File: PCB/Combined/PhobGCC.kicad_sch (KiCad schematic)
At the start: 74 parts, among them J1 Conn_01x06_Female, J2 Conn_01x04_Female, J3 Conn_01x01_Male, J4 Conn_01x04_Male, Q1 Q_NMOS_GSD, Q2 Q_PMOS_GDS, Q3 Q_NMOS_GSD, SW1 A, SW10 Dup, SW11 Dright, SW12 Ddown, SW2 B, SW3 X, SW4 Y, SW5 Start, SW6 L, SW7 R, SW9 Dleft, U1 Teensy4.0, U2 2x DRV5053CAQLPGM Hall Effect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, U3 GP2S60-MFG, U4 GP2S60-MFG, U5 Stickbox_Assembly

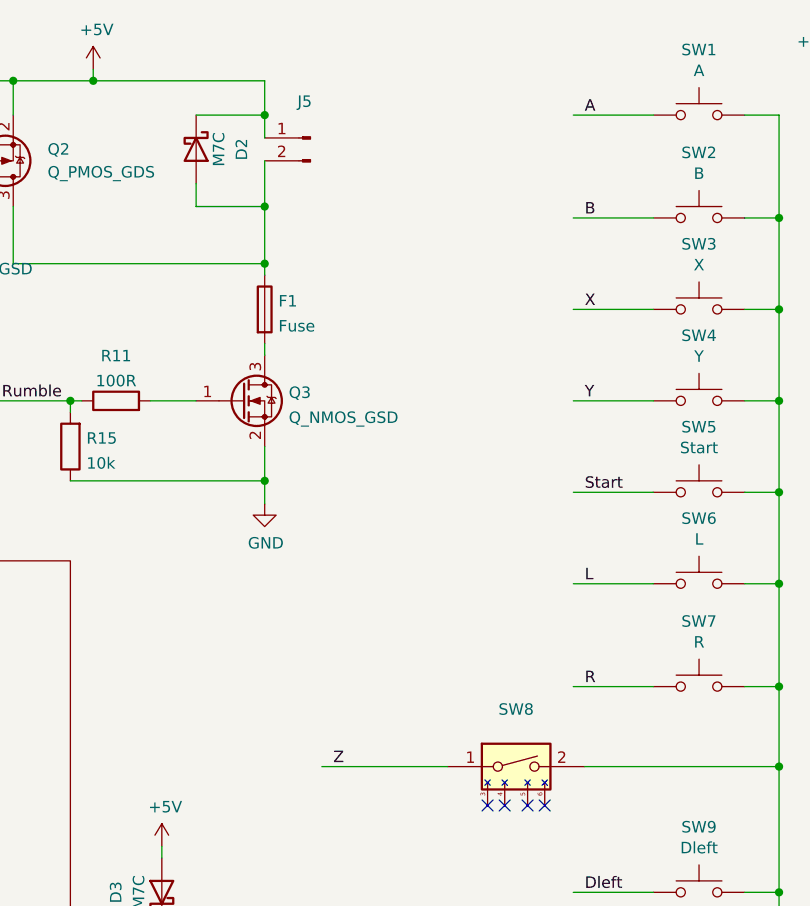
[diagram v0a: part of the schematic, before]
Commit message: applied footprint changes to all pcbs
forgot to change cstick and motherboard to reflect the new hall sensor footprint, fixed now.
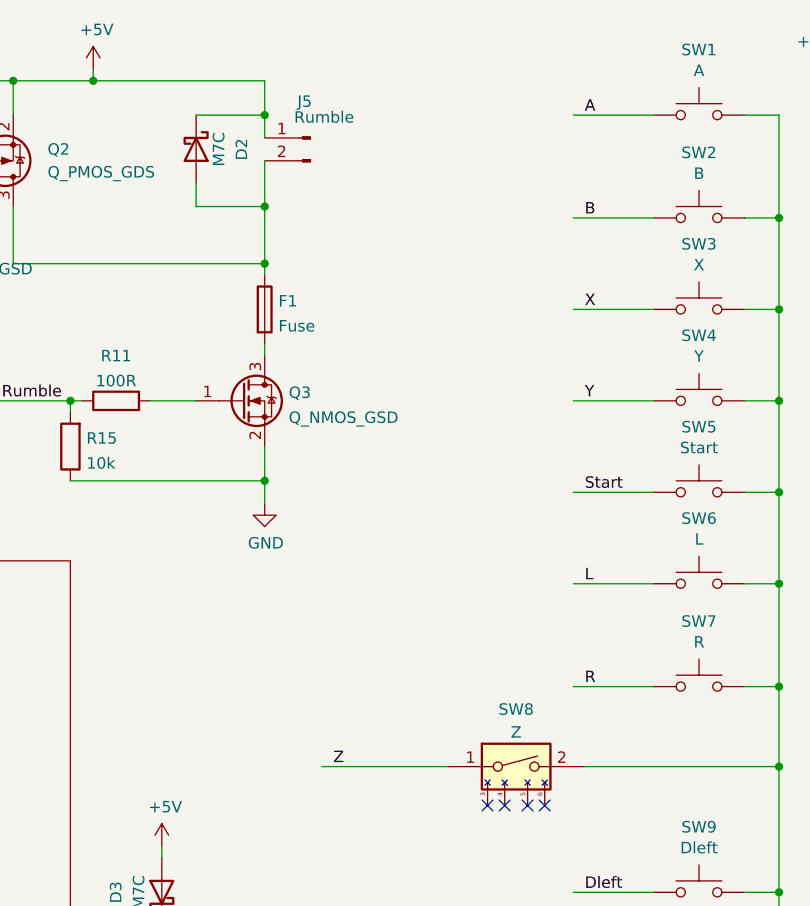
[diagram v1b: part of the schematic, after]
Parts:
- D1: footprint (none) -> PhobGCC_Footprints:D_SOD-523_Shorted
- H14, H15: footprint (none) -> PhobGCC_Footprints:breakaway-mousebites-double
- J5: value (none) -> Rumble; footprint (none) -> PhobGCC_Footprints:Pin_Header_Straight_1x02_Pitch2.54mm
- SW6, SW7: footprint (none) -> PhobGCC_Footprints:Pin_Header_Straight_1x02_Pitch2.54mm
- SW8: value (none) -> Z; footprint (none) -> PhobGCC_Footprints:Z_Switch_Edge
- U1: footprint (none) -> PhobGCC_Footprints:Teensy40_Edge_Pins
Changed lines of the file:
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@@
       (effects (font (size 1.524 1.524)))
     )
-    (property "Footprint" "" (id 2) (at 66.04 104.14 0)
+    (property "Footprint" "PhobGCC_Footprints:Teensy40_Edge_Pins" (id 2) (at 66.04 104.14 0)
       (effects (font (size 1.27 1.27)) hide)
     )
@@
     (property "Reference" "SW6" (id 0) (at 168.91 67.691 0))
     (property "Value" "L" (id 1) (at 168.91 70.0024 0))
-    (property "Footprint" "" (id 2) (at 168.91 69.85 0)
+    (property "Footprint" "PhobGCC_Footprints:Pin_Header_Straight_1x02_Pitch2.54mm" (id 2) (at 168.91 69.85 0)
       (effects (font (size 1.27 1.27)) hide)
     )
@@
     (property "Reference" "SW7" (id 0) (at 168.91 79.121 0))
     (property "Value" "R" (id 1) (at 168.91 81.4324 0))
-    (property "Footprint" "" (id 2) (at 168.91 81.28 0)
+    (property "Footprint" "PhobGCC_Footprints:Pin_Header_Straight_1x02_Pitch2.54mm" (id 2) (at 168.91 81.28 0)
       (effects (font (size 1.27 1.27)) hide)
     )
@@
     (in_bom yes) (on_board yes)
     (property "Reference" "SW8" (id 0) (at 148.59 88.9 0))
-    (property "Value" "" (id 1) (at 148.59 91.44 0))
-    (property "Footprint" "" (id 2) (at 148.59 95.25 0)
+    (property "Value" "Z" (id 1) (at 148.59 91.44 0))
+    (property "Footprint" "PhobGCC_Footprints:Z_Switch_Edge" (id 2) (at 148.59 95.25 0)
       (effects (font (size 1.27 1.27)) hide)
     )
@@
     (in_bom yes) (on_board yes)
     (property "Reference" "J5" (id 0) (at 125.095 21.3573 0))
-    (property "Value" "" (id 1) (at 127.254 23.114 0))
-    (property "Footprint" "" (id 2) (at 125.73 25.4 0)
+    (property "Value" "Rumble" (id 1) (at 127.254 23.114 0))
+    (property "Footprint" "PhobGCC_Footprints:Pin_Header_Straight_1x02_Pitch2.54mm" (id 2) (at 125.73 25.4 0)
       (effects (font (size 1.27 1.27)) hide)
     )
@@
       (effects (font (size 1.27 1.27)) (justify left))
     )
-    (property "Footprint" "" (id 2) (at 258.826 39.243 0)
+    (property "Footprint" "PhobGCC_Footprints:breakaway-mousebites-double" (id 2) (at 258.826 39.243 0)
       (effects (font (size 1.27 1.27)) hide)
     )
@@
       (effects (font (size 1.27 1.27)) (justify right))
     )
-    (property "Footprint" "" (id 2) (at 33.02 96.52 0)
+    (property "Footprint" "PhobGCC_Footprints:D_SOD-523_Shorted" (id 2) (at 33.02 96.52 0)
       (effects (font (size 1.27 1.27)) hide)
     )
@@
       (effects (font (size 1.27 1.27)) (justify left))
     )
-    (property "Footprint" "" (id 2) (at 258.826 44.958 0)
-      (effects (font (size 1.27 1.27)) hide)
-    )
+    (property "Footprint" "PhobGCC_Footprints:breakaway-mousebites-double" (id 2) (at 258.826 44.958 0)
+      (effects (font (size 1.27 1.27)) hide)
+    )
